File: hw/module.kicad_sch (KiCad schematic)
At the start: 33 parts, among them U1 CFPS-39, U2 CFPS-39, U3 74LVC1G125, U4 74 LVC 1G3157GW,125, U5 MAX919, U6 STM32L010F4P6, U7 BAS70-7-F

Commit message: Pcb++
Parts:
- added C15: 1n, Capacitor_SMD:C_0201_0603Metric_Pad0.64x0.40mm_HandSolder, symbol Device:C
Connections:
- net GND: now also C15.2
- net OSC_STAT: now also U6.3 (PC15-OSC32_OUT); no longer U6.2 (PC14-OSC32_IN)
- net RX: now also U6.14 (PB1), U6.18 (PA10); no longer U6.17 (PA9)
- net TX: now also U6.17 (PA9); no longer U6.18 (PA10)
- net at R8.2, U6.4 (NRST): now also C15.1
- no-connect marks 0 -> 7
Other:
- note added: "UART baurd rate measure"
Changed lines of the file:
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@@
   (junction (at 67.31 39.37) (diameter 0) (color 0 0 0 0)
   )
+  (junction (at 261.62 133.35) (diameter 0) (color 0 0 0 0)
+  )
   (junction (at 74.93 49.53) (diameter 0) (color 0 0 0 0)
   )
@@
   (junction (at 45.72 39.37) (diameter 0) (color 0 0 0 0)
   )
+  (no_connect (at 196.85 123.19))
+  (no_connect (at 196.85 125.73))
+  (no_connect (at 196.85 128.27))
+  (no_connect (at 196.85 130.81))
+  (no_connect (at 196.85 133.35))
+  (no_connect (at 196.85 135.89))
+  (no_connect (at 257.81 125.73))
   (wire (pts (xy 203.2 27.94) (xy 204.47 27.94))
     (stroke (width 0) (type default) (color 0 0 0 0))
@@
     (stroke (width 0) (type default) (color 0 0 0 0))
   )
+  (wire (pts (xy 261.62 147.32) (xy 261.62 133.35))
+    (stroke (width 0) (type default) (color 0 0 0 0))
+  )
   (wire (pts (xy 208.28 27.94) (xy 208.28 25.4))
     (stroke (width 0) (type default) (color 0 0 0 0))
@@
     (stroke (width 0) (type default) (color 0 0 0 0))
   )
-  (wire (pts (xy 257.81 133.35) (xy 273.05 133.35))
+  (wire (pts (xy 257.81 133.35) (xy 261.62 133.35))
     (stroke (width 0) (type default) (color 0 0 0 0))
   )
@@
     (stroke (width 0) (type default) (color 0 0 0 0))
   )
+  (wire (pts (xy 261.62 133.35) (xy 273.05 133.35))
+    (stroke (width 0) (type default) (color 0 0 0 0))
+  )
   (wire (pts (xy 83.82 38.1) (xy 83.82 29.21))
     (stroke (width 0) (type default) (color 0 0 0 0))
@@
     (stroke (width 0) (type default) (color 0 0 0 0))
   )
-  (wire (pts (xy 257.81 125.73) (xy 262.89 125.73))
-    (stroke (width 0) (type default) (color 0 0 0 0))
-  )
   (wire (pts (xy 60.96 81.28) (xy 60.96 82.55))
     (stroke (width 0) (type default) (color 0 0 0 0))
@@
   (wire (pts (xy 231.14 33.02) (xy 241.3 33.02))
     (stroke (width 0) (type default) (color 0 0 0 0))
+  )
+  (text "UART baurd rate measure" (at 251.46 115.57 0)
+    (effects (font (size 1.27 1.27)) (justify left bottom))
   )
   (label "OSC" (at 194.31 118.11 0)
@@
     (effects (font (size 1.27 1.27)) (justify left bottom))
   )
-  (label "TX" (at 191.77 140.97 0)
+  (label "RX" (at 257.81 118.11 0)
     (effects (font (size 1.27 1.27)) (justify left bottom))
   )
-  (label "RX" (at 191.77 138.43 0)
+  (label "TX" (at 191.77 138.43 0)
+    (effects (font (size 1.27 1.27)) (justify left bottom))
+  )
+  (label "RX" (at 191.77 140.97 0)
     (effects (font (size 1.27 1.27)) (justify left bottom))
   )
@@
     (effects (font (size 1.27 1.27)) (justify right bottom))
   )
-  (label "OSC_STAT" (at 262.89 125.73 0)
+  (label "OSC_STAT" (at 257.81 128.27 0)
     (effects (font (size 1.27 1.27)) (justify left bottom))
   )
@@
       (effects (font (size 1.27 1.27)) hide)
     )
-    (property "Datasheet" "https://foxonline.com/wp-content/uploads/pdfs/T5HN_T5HV.pdf" (id 3) (at 33.02 31.75 0)
+    (property "Datasheet" "https://www.farnell.com/datasheets/3161535.pdf" (id 3) (at 33.02 31.75 0)
       (effects (font (size 1.27 1.27)) hide)
     )
@@
     )
     (property "Datasheet" "~" (id 3) (at 86.36 185.42 0)
+      (effects (font (size 1.27 1.27)) hide)
+    )
+    (pin "1")
+    (pin "2")
+  )
+  (symbol (lib_id "Device:C") (at 261.62 151.13 0) (unit 1)
+    (in_bom yes) (on_board yes)
+    (property "Reference" "C15" (id 0) (at 261.62 148.59 0)
+      (effects (font (size 1.27 1.27)) (justify left))
+    )
+    (property "Value" "1n" (id 1) (at 261.62 153.67 0)
+      (effects (font (size 1.27 1.27)) (justify left))
+    )
+    (property "Footprint" "Capacitor_SMD:C_0201_0603Metric_Pad0.64x0.40mm_HandSolder" (id 2) (at 262.5852 154.94 0)
+      (effects (font (size 1.27 1.27)) hide)
+    )
+    (property "Datasheet" "~" (id 3) (at 261.62 151.13 0)
       (effects (font (size 1.27 1.27)) hide)
     )
@@
       (effects (font (size 1.27 1.27)) hide)
     )
-    (property "Datasheet" "https://foxonline.com/wp-content/uploads/pdfs/T5HN_T5HV.pdf" (id 3) (at 33.02 60.96 0)
+    (property "Datasheet" "https://www.farnell.com/datasheets/3161535.pdf" (id 3) (at 33.02 60.96 0)
       (effects (font (size 1.27 1.27)) hide)
     )
@@
     (pin "1")
   )
+  (symbol (lib_id "power:GND") (at 261.62 154.94 0) (unit 1)
+    (in_bom yes) (on_board yes) (fields_autoplaced)
+    (property "Reference" "#PWR0148" (id 0) (at 261.62 161.29 0)
+      (effects (font (size 1.27 1.27)) hide)
+    )
+    (property "Value" "GND" (id 1) (at 261.62 160.02 0))
+    (property "Footprint" "" (id 2) (at 261.62 154.94 0)
+      (effects (font (size 1.27 1.27)) hide)
+    )
+    (property "Datasheet" "" (id 3) (at 261.62 154.94 0)
+      (effects (font (size 1.27 1.27)) hide)
+    )
+    (pin "1")
+  )
   (sheet_instances
     (path "/" (page "1"))
@@
       (reference "#PWR0147") (unit 1) (value "GND") (footprint "")
     )
+    (path "/ff3224f2-597f-4de0-b990-ceb1092ce4d1"
+      (reference "#PWR0148") (unit 1) (value "GND") (footprint "")
+    )
     (path "/dba28061-2a05-48de-9ce8-c1981fd46f77"
       (reference "C1") (unit 1) (value "10n") (footprint "Capacitor_SMD:C_0201_0603Metric_Pad0.64x0.40mm_HandSolder")
@@
       (reference "C14") (unit 1) (value "100n") (footprint "Capacitor_SMD:C_0805_2012Metric_Pad1.18x1.45mm_HandSolder")
     )
+    (path "/900d0f64-503c-4ece-92c9-4e4a50c42589"
+      (reference "C15") (unit 1) (value "1n") (footprint "Capacitor_SMD:C_0201_0603Metric_Pad0.64x0.40mm_HandSolder")
+    )
     (path "/5460b77d-1803-489d-8702-1c9b3487aa2e"

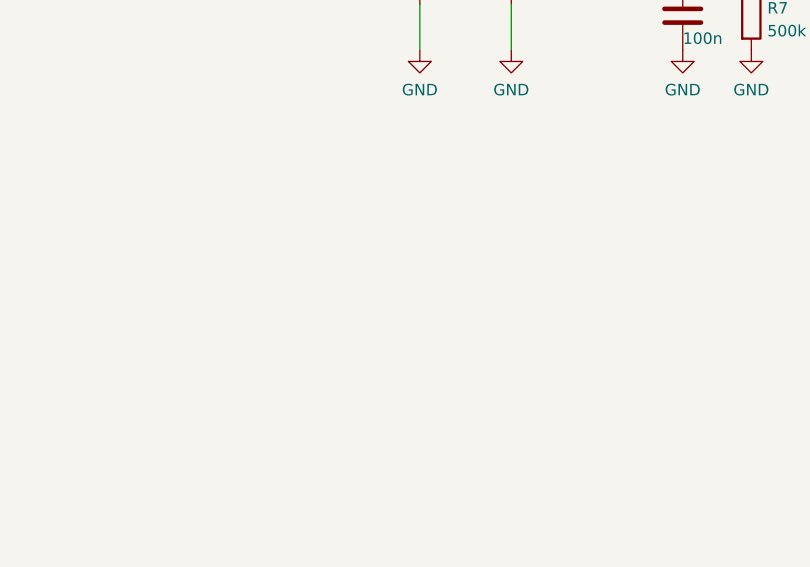
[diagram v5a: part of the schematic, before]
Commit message: Add 3D models
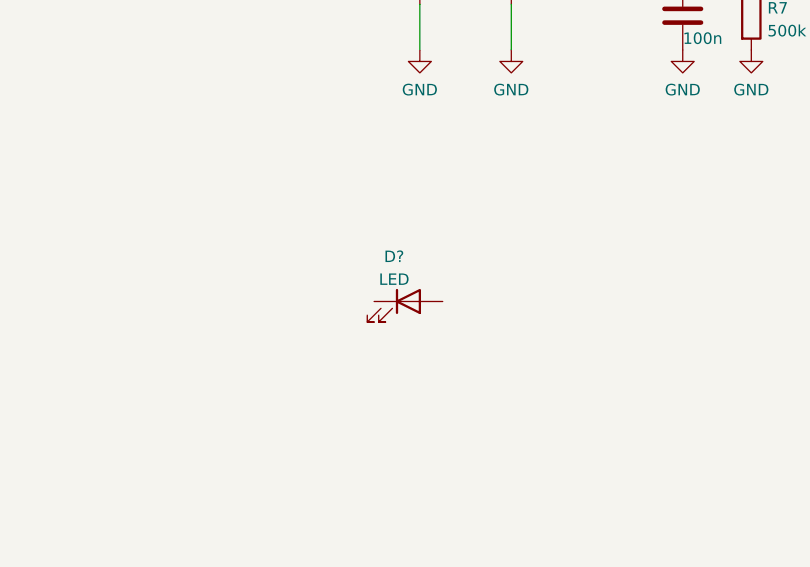
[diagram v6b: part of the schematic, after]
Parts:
- added D?: LED, symbol Device:LED
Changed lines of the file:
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@@
+    (pin "2")
+  )
+  (symbol (lib_id "Device:LED") (at 193.04 68.58 0) (unit 1)
+    (in_bom yes) (on_board yes) (fields_autoplaced)
+    (property "Reference" "D?" (id 0) (at 191.4525 63.6102 0))
+    (property "Value" "LED" (id 1) (at 191.4525 66.1471 0))
+    (property "Footprint" "" (id 2) (at 193.04 68.58 0)
+      (effects (font (size 1.27 1.27)) hide)
+    )
+    (property "Datasheet" "~" (id 3) (at 193.04 68.58 0)
+      (effects (font (size 1.27 1.27)) hide)
+    )
+    (pin "1")
     (pin "2")
   )
@@
       (reference "C15") (unit 1) (value "1n") (footprint "Capacitor_SMD:C_0201_0603Metric_Pad0.64x0.40mm_HandSolder")
     )
+    (path "/e3d22044-b494-47c6-a91c-b875387e7184"
+      (reference "D?") (unit 1) (value "LED") (footprint "")
+    )
     (path "/5460b77d-1803-489d-8702-1c9b3487aa2e"

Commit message: Footprint fix, and first PCB release
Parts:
- removed D?: LED, symbol Device:LED
- added C16, C17, C18, C19, C20, C21: 4u7, Capacitor_SMD:C_0402_1005Metric_Pad0.74x0.62mm_HandSolder, symbol Device:C
- added C22: 200p, Capacitor_SMD:C_0201_0603Metric_Pad0.64x0.40mm_HandSolder, symbol Device:C
- added Q1: MUN 2211, Package_TO_SOT_SMD:SOT-23_Handsoldering, symbol Device:Q_NPN_BEC_BRT
- added R11, R12: 150k, Resistor_SMD:R_0201_0603Metric_Pad0.64x0.40mm_HandSolder, symbol Device:R
- added R9: 100, Resistor_SMD:R_0201_0603Metric_Pad0.64x0.40mm_HandSolder, symbol Device:R
- added U8: SS39ET, Package_TO_SOT_SMD:SOT-23_Handsoldering, symbol Sensor_Current:A1363xKTTN-1
- L1: value L -> 27n
- R5: value R -> 10
- U1, U2: footprint Oscillator:Oscillator_SMD_Fox_FT5H_5.0x3.2mm -> Oscillator:Oscillator_SMD_EuroQuartz_XO32-4Pin_3.2x2.5mm_HandSoldering
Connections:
- net +3.3V: now also R11.1, U8.1 (VCC)
- net GND: now also C16.2, C17.2, C18.2, C19.2, C20.2, C21.2, C22.2, Q1.2 (E)
- net hall_on: now reaches U6.2 (PC14-OSC32_IN)
- net hall_on: now also Q1.1 (B)
- net hall_exp: now reaches U6.8 (PA2)
- net hall_exp: now also C22.1, R9.2
- net Cap_experiment: now reaches U6.9 (PA3)
- net Cap_experiment: now also C16.1, C17.1, C18.1, C19.1, C20.1, C21.1, R12.2
- new net: Q1.3 (C), U8.3 (NC)
- new net: R11.2, R12.1
- new net: R9.1, U8.2 (VOUT)
- no-connect marks 7 -> 4

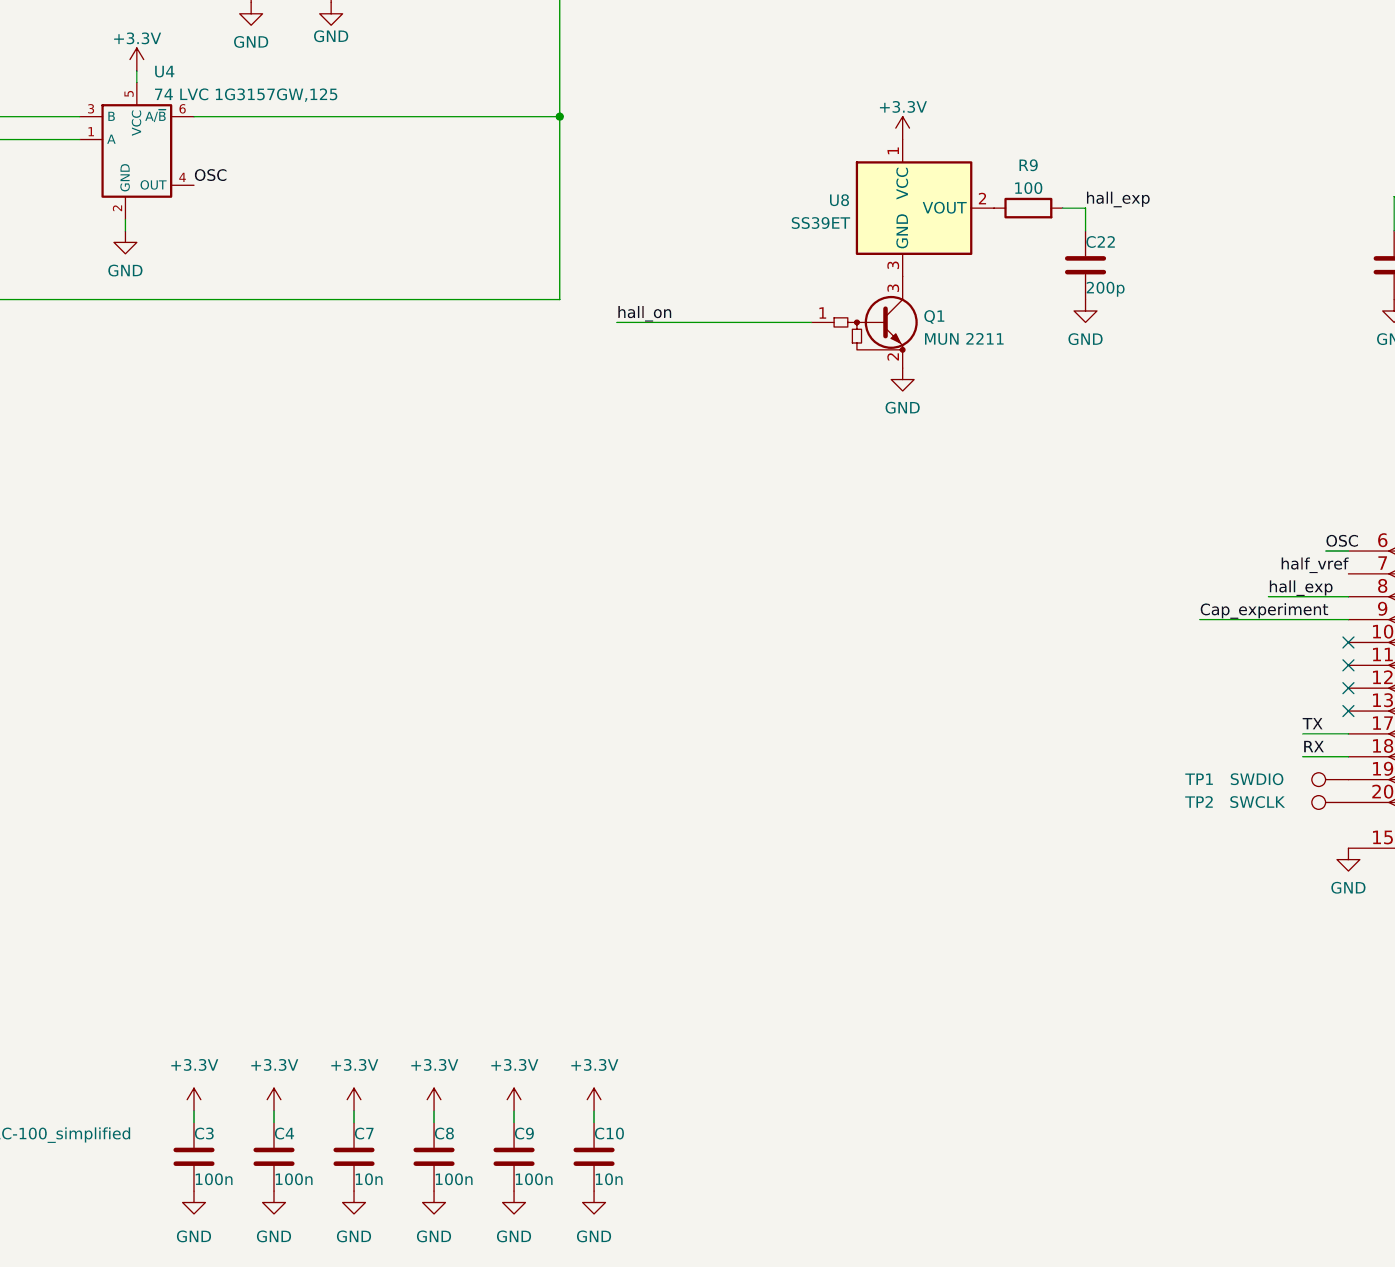
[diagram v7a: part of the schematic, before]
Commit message: Final 3D models, final capacitor sizes, final capacitor numbers, final capacitor placements
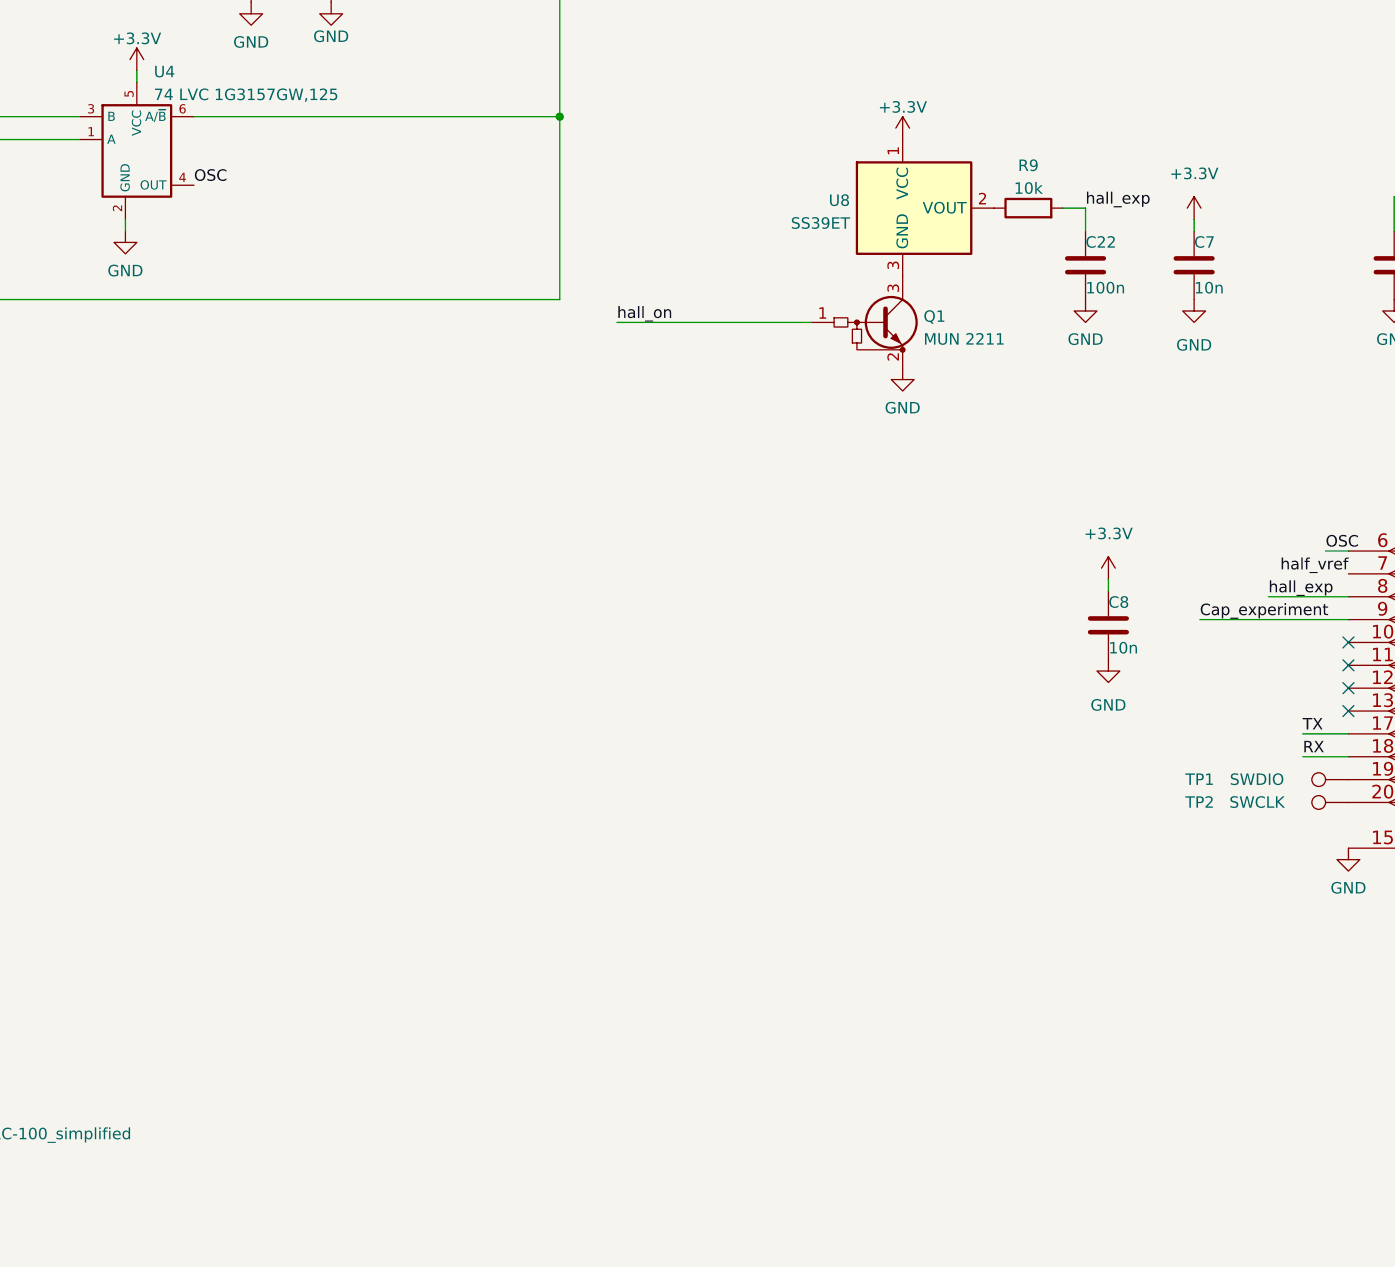
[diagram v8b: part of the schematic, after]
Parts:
- removed C10: 10n, Capacitor_SMD:C_0201_0603Metric_Pad0.64x0.40mm_HandSolder, symbol Device:C
- removed C3, C4, C9: 100n, Capacitor_SMD:C_0201_0603Metric_Pad0.64x0.40mm_HandSolder, symbol Device:C
- C11, C12, C13, C14: footprint Capacitor_SMD:C_0805_2012Metric_Pad1.18x1.45mm_HandSolder -> Capacitor_SMD:C_0201_0603Metric_Pad0.64x0.40mm_HandSolder
- C22: value 200p -> 100n
- C8: value 100n -> 10n
- R9: value 100 -> 10k
- U1, U2: footprint Oscillator:Oscillator_SMD_EuroQuartz_XO32-4Pin_3.2x2.5mm_HandSoldering -> farnell:Oscillator_SMD_EuroQuartz_XO32-4Pin_3.2x2.5mm_HandSoldering
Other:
- moved on the sheet: C7, C8
